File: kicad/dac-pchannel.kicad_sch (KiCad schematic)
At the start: 10 parts, among them Q1 SI2307DS, Q2 SI2304DS

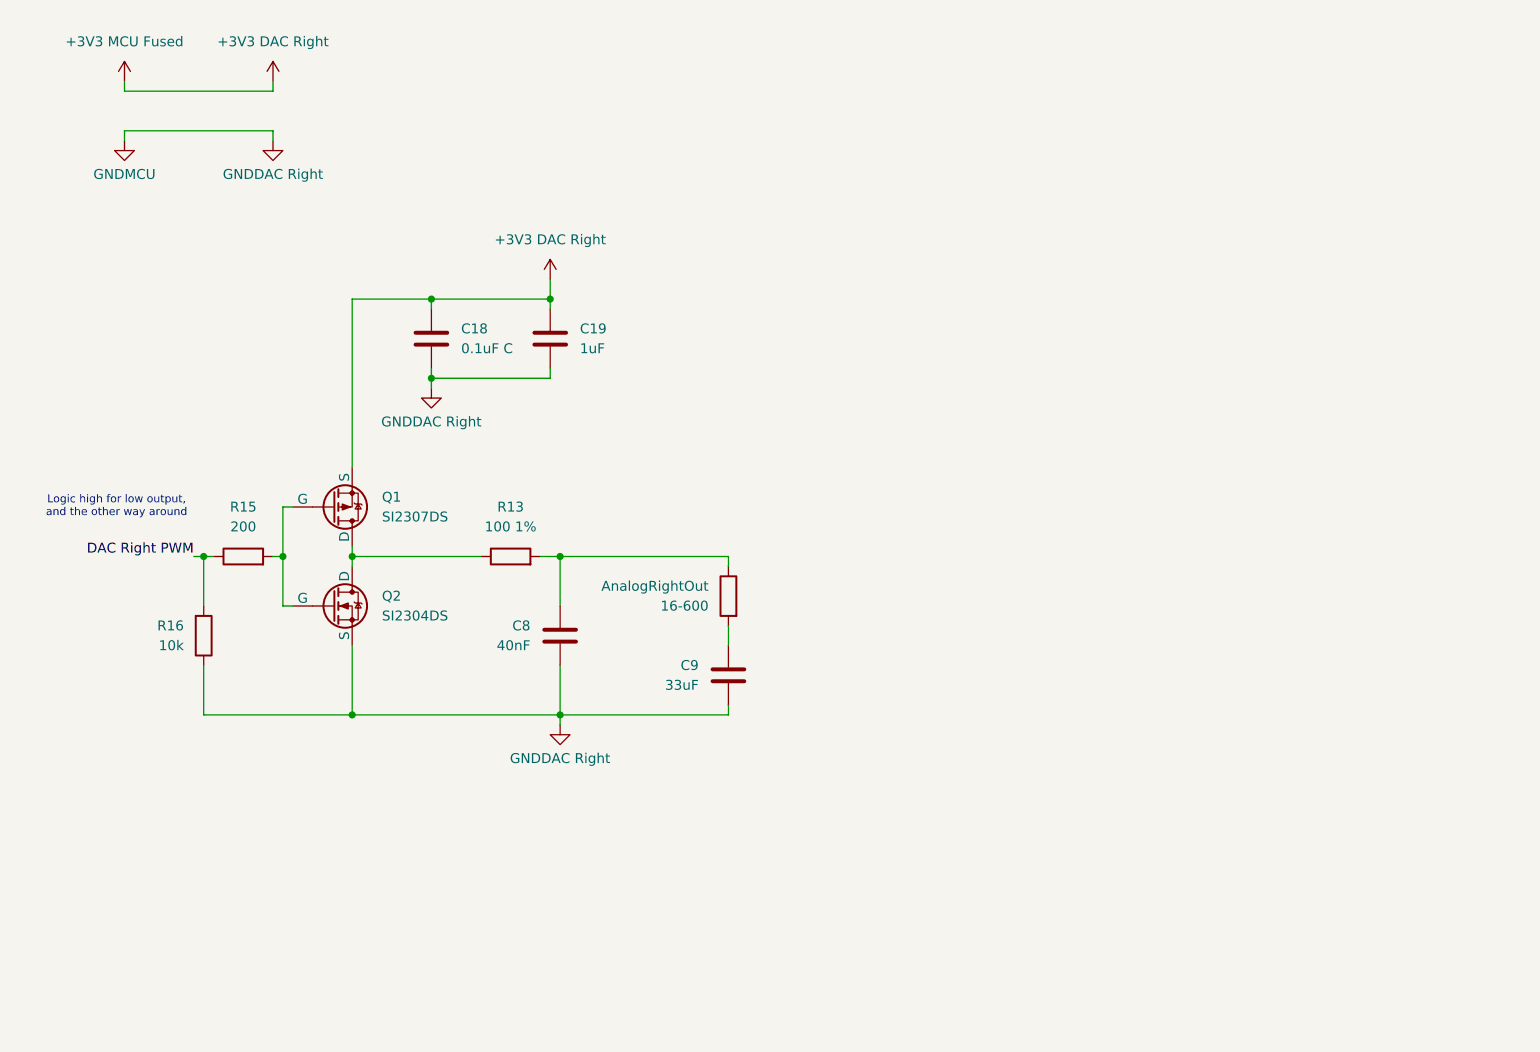
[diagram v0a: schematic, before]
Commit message: Stereo schematic, code cleanup
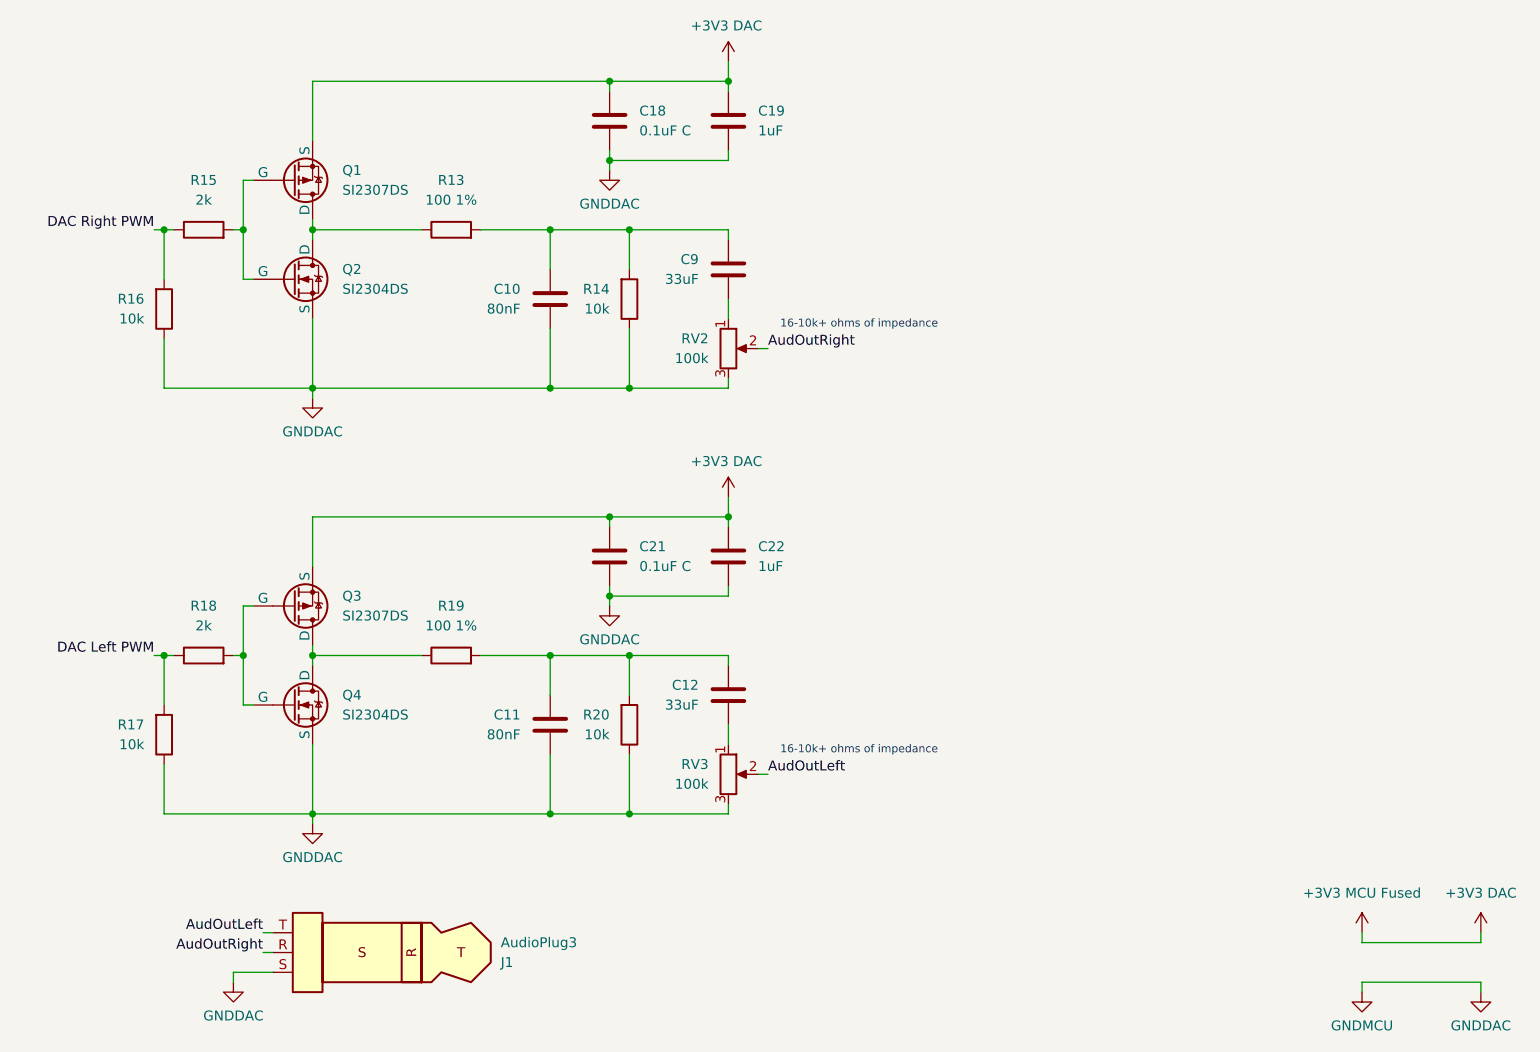
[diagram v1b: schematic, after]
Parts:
- removed AnalogRightOut: 16-600, symbol Device:R
- removed C8: 40nF, symbol Device:C
- added C10, C11: 80nF, symbol Device:C
- added C12: 33uF, symbol Device:C
- added C21: 0.1uF C, symbol Device:C
- added C22: 1uF, symbol Device:C
- added J1: AudioPlug3, symbol Connector_Audio:AudioPlug3
- added Q3: SI2307DS, symbol Simulation_SPICE:PMOS
- added Q4: SI2304DS, symbol Simulation_SPICE:NMOS
- added R14, R17, R20: 10k, symbol Device:R
- added R18: 2k, symbol Device:R
- added R19: 100 1%, symbol Device:R
- added RV2, RV3: 100k, symbol Device:R_Potentiometer
- R15: value 200 -> 2k
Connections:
- net at R13.2: now also C9.1, C10.1, R14.2
- net +3V3 DAC Right renamed +3V3 DAC
- net +3V3 DAC: now also C21.1, C22.1, Q3.3 (S)
- net GNDDAC Right renamed GNDDAC
- net GNDDAC: now also C10.2, C11.2, C21.2, C22.2, J1.S, Q4.3 (S), R14.1, R17.1, R20.1, RV2.3, RV3.3; no longer C9.2
- new net: Q3.2 (G), Q4.2 (G), R18.2
- new net: Q3.1 (D), Q4.1 (D), R19.1
- new net: C9.2, RV2.1
- new net: C11.1, C12.1, R19.2, R20.2
- new net: C12.2, RV3.1
- new net AudOutLeft: J1.T, RV3.2
- new net AudOutRight: J1.R, RV2.2
- new net DAC Left PWM: R17.2, R18.1
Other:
- note added: "16-10k+ ohms of impedance"
- note removed: "Logic high for low output, and the other way around"
- moved on the sheet: C18, C19, C9, Q1, Q2, R13, R16
